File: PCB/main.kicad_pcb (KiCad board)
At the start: 2 copper layers, 76.5 x 37.5 mm, 16 parts, among them J1 USB_C_Receptacle, J2 RJ45, J3 USB_C_Receptacle, J4 USB_C_Receptacle, M1 Fan_PC_Chassis, M2 Fan_PC_Chassis, M3 Fan_PC_Chassis, M4 Fan_PC_Chassis, SW1 SW_DPDT_x2, U2 LAN9512i

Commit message: fixing PCB
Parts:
- added R6: R, Resistor_SMD:R_0815_2038Metric, F.Cu at (177.8, 71.8)
- moved J1 22.7 mm to (148.0, 56.8), turned to 180 degrees
- moved J4 12.4 mm to (136.5, 57.0), turned to 180 degrees
- moved J3 12.3 mm to (125.0, 57.0), turned to 180 degrees
- moved J2 2.76 mm to (167.5, 65.3)
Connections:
- J1 pad A5: unconnected-(J1-CC1-PadA5) -> Net-(J1-CC1)
- J1 pad B5: unconnected-(J1-CC2-PadB5) -> Net-(J1-CC2)
- J1 pad S1: unconnected-(J1-SHIELD-PadS1) -> gnd
- J3 pad S1: unconnected-(J3-SHIELD-PadS1) -> gnd
- J4 pad S1: unconnected-(J4-SHIELD-PadS1) -> gnd
- R7 pad 2: unconnected-(R7-Pad2) -> Net-(J1-CC1)
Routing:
- net gnd: track 101.2 -> 301.4 mm, vias 2 -> 6
- net Net-(J4-CC2): track 128.5 -> 27.5 mm
- net Net-(J1-CC2): track 0.00 -> 86.9 mm
- net VBUSUP: track 94.2 -> 52.0 mm, vias 0 -> 2
- net Net-(J1-CC1): track 0.00 -> 35.0 mm, vias 0 -> 2
- net D-DOWN2: track 64.1 -> 34.6 mm, vias 1 -> 0
- net D+DOWN2: track 75.9 -> 47.0 mm
- net D-DOWN1: track 54.7 -> 31.0 mm, vias 1 -> 0
- net D+UP: track 46.3 -> 33.2 mm, vias 0 -> 1
- net Net-(J3-CC2): track 33.4 -> 24.3 mm
- net D+DOWN1: track 59.9 -> 54.7 mm, vias 1 -> 0
- net Net-(U2B-PRTCTL2): track 99.2 -> 95.1 mm
- net Net-(U2B-TXP): track 45.1 -> 48.2 mm
- net Net-(U2B-RXP): track 38.0 -> 35.7 mm
- net unconnected-(R7-Pad2): track 2.04 -> 0.00 mm
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
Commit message: fixing things
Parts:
- added Y2: KC2520Z, Oscillator:Oscillator_SMD_Kyocera_KC2520Z-4Pin_2.5x2.0mm, F.Cu at (157.0, 87.1)
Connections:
- U2 pad 61: unconnected-(U2A-XI-Pad61) -> Net-(U2A-XI)
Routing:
- net VBUSUP: track 52.0 -> 107.4 mm, vias 2 -> 6
- net Net-(U2A-XI): track 0.00 -> 39.3 mm, vias 0 -> 2
- net gnd: track 301.4 -> 308.6 mm
- net Net-(U2B-USBRBIAS): track 52.5 -> 51.3 mm
- net Net-(U2B-PRTCTL2): track 95.1 -> 95.9 mm

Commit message: fixing lots of things
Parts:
- removed J2: RJ45, Connector_RJ:RJ45_Amphenol_54602-x08_Horizontal
- added C1: 0.1 pF, Capacitor_SMD:C_0201_0603Metric, F.Cu at (138.2, 69.2)
- added C10: 0.1, Capacitor_SMD:C_0201_0603Metric, F.Cu at (138.8, 79.8)
- added C11: 4.7, Capacitor_SMD:C_0201_0603Metric, F.Cu at (153.7, 83.8)
- added C2: 33 pF, Capacitor_SMD:C_0201_0603Metric, F.Cu at (138.0, 70.8)
- added C3: 0.1, Capacitor_SMD:C_0201_0603Metric, F.Cu at (169.2, 81.0)
- added C4: 0.1, Capacitor_SMD:C_0201_0603Metric, F.Cu at (154.8, 77.1)
- added C5: 0.1 uF, Capacitor_SMD:C_0201_0603Metric, F.Cu at (125.7, 62.5)
- added C6: 330, Capacitor_SMD:C_0201_0603Metric, F.Cu at (147.8, 63.8)
- added C8: 1.0, Capacitor_SMD:C_0201_0603Metric, F.Cu at (135.8, 73.8)
- added C9: 0.1, Capacitor_SMD:C_0201_0603Metric, F.Cu at (154.2, 80.8)
- added FB1: FerriteBead, Inductor_SMD:L_Ferrocore_DLG-0302, F.Cu at (158.8, 67.2)
- added J6: RJ45_Amphenol_RJMG1BD3B8K1ANR, Connector_RJ:RJ45_Amphenol_RJMG1BD3B8K1ANR, F.Cu at (176.9, 65.4)
- added R10: 10, Resistor_SMD:R_0201_0603Metric, F.Cu at (168.5, 74.0)
- added R11: 10, Resistor_SMD:R_0201_0603Metric, F.Cu at (165.7, 72.0)
- added R12: 10, Resistor_SMD:R_0201_0603Metric, F.Cu at (153.6, 69.0)
- added R13: 10, Resistor_SMD:R_0201_0603Metric, F.Cu at (176.1, 71.5)
- added R14: 10, Resistor_SMD:R_0201_0603Metric, F.Cu at (169.2, 76.5)
- added R15: 330, Resistor_SMD:R_0201_0603Metric, F.Cu at (125.5, 56.3)
- added R16: 0.1 uF, Resistor_SMD:R_0201_0603Metric, F.Cu at (147.8, 62.8)
- added R17: 39.2 K, Resistor_SMD:R_0201_0603Metric, F.Cu at (146.7, 84.5)
- added R18: 61.9 K, Resistor_SMD:R_0201_0603Metric, F.Cu at (138.5, 83.3)
- added R8: 1.0 M, Resistor_SMD:R_0201_0603Metric, F.Cu at (143.2, 71.5)
- added R9: 12.4k, Resistor_SMD:R_0201_0603Metric, F.Cu at (149.2, 71.2)
- R1, R2, R3, R4: value R -> 5.1k; footprint Resistor_SMD:R_0815_2038Metric -> Resistor_SMD:R_0201_0603Metric
- R5: value R -> 12.0 k; footprint Resistor_SMD:R_0815_2038Metric -> Resistor_SMD:R_0201_0603Metric
- R6, R7: footprint Resistor_SMD:R_0815_2038Metric -> Resistor_SMD:R_0201_0603Metric
- moved SW1 61.4 mm to (112.6, 54.8), turned to -90 degrees
- moved M1 41.1 mm to (110.2, 85.4)
- moved R5 33.3 mm to (141.5, 72.2)
- moved R1 31.7 mm to (143.2, 66.2), turned to 180 degrees
- moved R4 30.3 mm to (145.5, 66.2), turned to 180 degrees
- moved R6 26.3 mm to (153.0, 63.0)
- moved Y2 23.6 mm to (140.8, 70.0), turned to 90 degrees
- moved M2 21.6 mm to (119.2, 77.9)
- moved R7 20.8 mm to (156.8, 62.8), turned to 180 degrees
- moved M3 19.6 mm to (119.2, 85.4)
- moved J3 18.8 mm to (143.8, 56.2)
- moved R2 17.7 mm to (127.5, 64.5)
- moved R3 17.5 mm to (134.2, 64.0), turned to 180 degrees
- moved M4 13.9 mm to (110.2, 77.9)
- moved J1 7.26 mm to (155.2, 56.2)
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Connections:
- net Net-(U2A-VDD33A-Pad10) renamed VDD33A
- J3 pad S1: gnd -> Net-(J3-SHIELD)
- J4 pad S1: gnd -> Net-(J4-SHIELD)
- U2 pad 11: VBUSUP -> Net-(U2B-VBUS_DET)
- U2 pad 34: unconnected-(U2A-TEST2-Pad34) -> gnd
- U2 pad 40: unconnected-(U2A-TEST3-Pad40) -> VBUSUP
- U2 pad 48: unconnected-(U2A-VDD18ETHPLL-Pad48) -> Net-(U2A-VDD18ETHPLL)
- U2 pad 50: unconnected-(U2B-EXRES-Pad50) -> Net-(U2B-EXRES)
- U2 pad 62: unconnected-(U2A-VDD18USBPLL-Pad62) -> Net-(U2A-VDD18USBPLL)
- Y2 pad 1: gnd -> Net-(Y2-GND)
- Y2 pad 2: gnd -> Net-(Y2-GND)
- Y2 pad 4: VBUSUP -> Net-(Y2-VCC)
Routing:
- net VDD33A: track 0.00 -> 156.7 mm, vias 0 -> 3
- net Net-(J1-CC2): track 86.9 -> 13.3 mm, vias 0 -> 2
- net Net-(U2B-PRTCTL2): track 95.9 -> 40.8 mm, vias 0 -> 2
- net VBUSUP: track 107.4 -> 157.4 mm, vias 6 -> 7
- net Net-(U2B-USBRBIAS): track 51.3 -> 1.84 mm, vias 2 -> 0
- net Net-(J4-SHIELD): track 0.00 -> 39.6 mm
- net Net-(U2A-VDD18USBPLL): track 0.00 -> 36.4 mm, vias 0 -> 3
- net Net-(J4-CC1): track 38.8 -> 3.12 mm, vias 2 -> 0
- net Net-(U2A-XI): track 39.3 -> 5.29 mm, vias 2 -> 0
- net Net-(J1-CC1): track 35.0 -> 1.85 mm, vias 2 -> 0
- net Net-(J3-SHIELD): track 0.00 -> 28.2 mm, vias 0 -> 2
- net D-DOWN1: track 31.0 -> 51.1 mm, vias 0 -> 4
- net Net-(J6-RCT): track 0.00 -> 18.8 mm, vias 0 -> 1
- net Net-(C10-Pad2): track 24.4 -> 43.0 mm
- net Net-(U2B-VBUS_DET): track 0.00 -> 17.6 mm, vias 0 -> 2
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
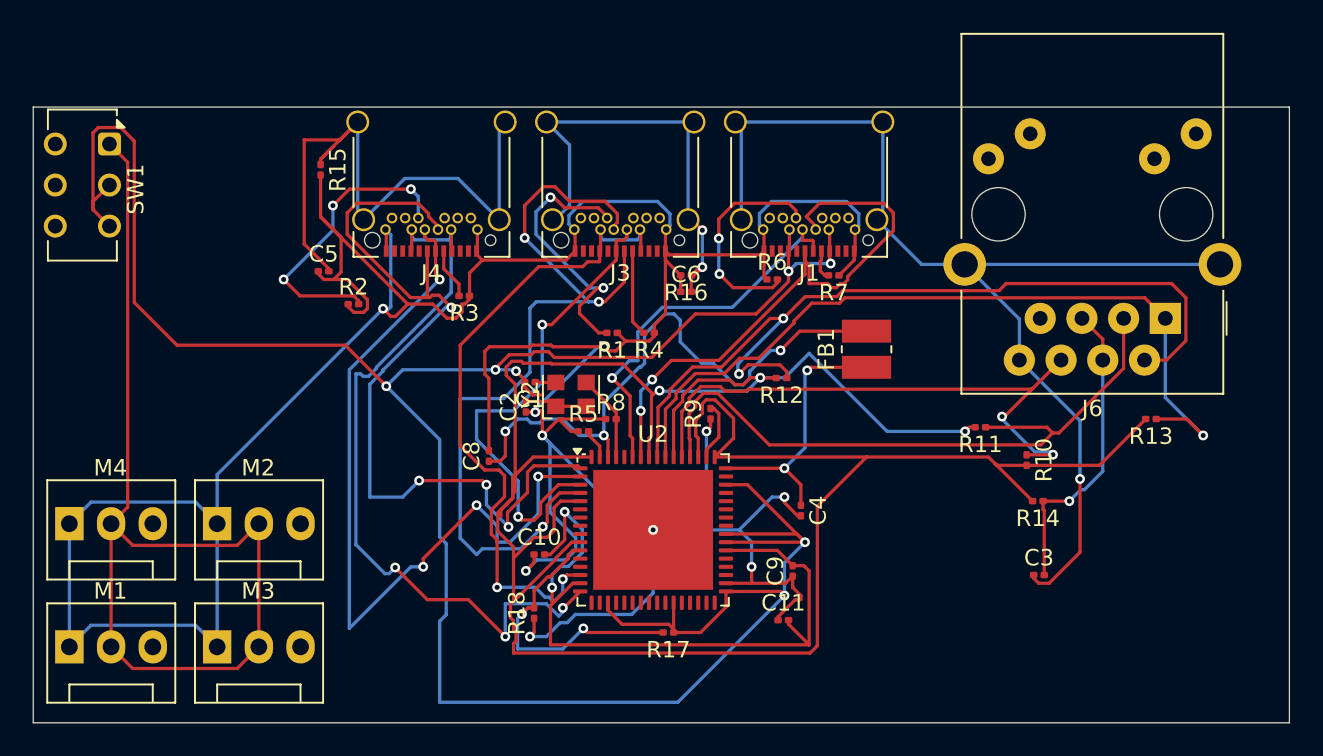
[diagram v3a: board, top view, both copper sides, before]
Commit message: fixing caps
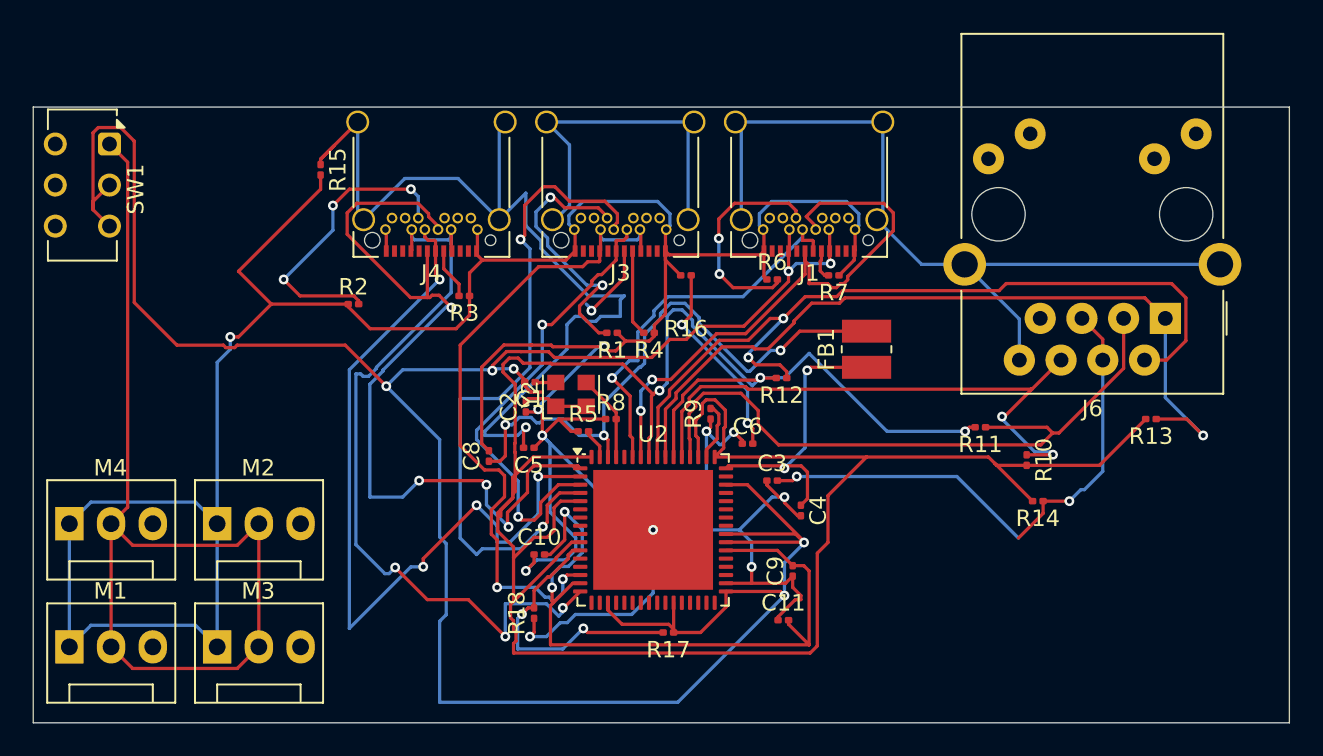
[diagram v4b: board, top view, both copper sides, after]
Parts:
- moved C3 17.2 mm to (153.0, 75.2)
- moved C5 16.5 mm to (138.2, 73.2), turned to 180 degrees
- moved C6 9.98 mm to (151.5, 73.0)
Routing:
- net gnd: track 303.5 -> 280.5 mm
- net Net-(J4-SHIELD): track 39.6 -> 57.4 mm, vias 0 -> 1
- net Net-(J6-RCT): track 18.8 -> 33.4 mm, vias 1 -> 2
- net VDD33A: track 156.7 -> 163.0 mm
- net Net-(J3-SHIELD): track 28.2 -> 34.4 mm
- net D+DOWN2: track 50.8 -> 46.5 mm
- net Net-(J6-TD-): track 52.8 -> 50.9 mm
- net Net-(U2A-VDD18ETHPLL): track 16.5 -> 17.7 mm
- net D-DOWN2: track 29.4 -> 28.2 mm

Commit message: fixing things
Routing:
- net Net-(J6-RCT): vias 2 -> 3
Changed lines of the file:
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@@
+		(net 18)
+	)
+	(via
+		(at 168 78.75)
+		(size 0.6)
+		(drill 0.3)
+		(layers "F.Cu" "B.Cu")
 		(net 18)
 	)

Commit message: fixing things
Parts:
- added C7: 0.1 uF, Capacitor_SMD:C_0201_0603Metric, F.Cu at (151.7, 82.8)
- added R19: 330, Resistor_SMD:R_0201_0603Metric, F.Cu at (151.7, 84.5)
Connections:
- J1 pad S1: gnd -> Net-(J1-SHIELD)
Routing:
- net Net-(J1-SHIELD): track 0.00 -> 99.5 mm, vias 0 -> 1
- net gnd: track 280.5 -> 257.1 mm

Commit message: fixing things
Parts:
- removed J3: USB_C_Receptacle, Connector_USB:USB_C_Receptacle_Amphenol_12401548E4-2A_CircularHoles
- added J2: USB_C_Receptacle, footprintsweeeeee:12401826_AMP, F.Cu at (143.9, 54.1)
- J1, J4: footprint Connector_USB:USB_C_Receptacle_Amphenol_12401548E4-2A_CircularHoles -> footprintsweeeeee:12401826_AMP
- moved J4 2.15 mm to (132.5, 54.1)
- moved J1 2.14 mm to (155.4, 54.1)
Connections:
- C5 pad 2: Net-(J4-SHIELD) -> Net-(C5-Pad2)
- C7 pad 2: Net-(J1-SHIELD) -> Net-(C7-Pad2)
- J1 pad S1: Net-(J1-SHIELD) -> Net-(C7-Pad2)
- J4 pad S1: Net-(J4-SHIELD) -> Net-(C5-Pad2)
- R15 pad 1: Net-(J4-SHIELD) -> Net-(C5-Pad2)
- R19 pad 1: Net-(J1-SHIELD) -> Net-(C7-Pad2)
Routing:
- net Net-(J1-SHIELD): track 99.5 -> 0.00 mm, vias 1 -> 0
- net Net-(C7-Pad2): track 0.00 -> 94.2 mm, vias 0 -> 4
- net Net-(J4-SHIELD): track 57.4 -> 0.00 mm, vias 1 -> 0
- net Net-(C5-Pad2): track 0.00 -> 38.0 mm, vias 0 -> 4
- net VBUSUP: track 157.9 -> 129.3 mm, vias 7 -> 8
- net gnd: track 257.1 -> 282.0 mm
- net D-DOWN1: track 51.1 -> 27.4 mm
- net Net-(U2B-PRTCTL2): track 40.8 -> 61.7 mm
- net D+DOWN1: track 49.1 -> 32.4 mm, vias 4 -> 5
- net D-DOWN2: track 28.2 -> 42.7 mm, vias 2 -> 3
- net Net-(J4-CC2): track 18.2 -> 12.6 mm, vias 3 -> 2
- net Net-(U2A-VDD18USBPLL): track 35.9 -> 41.4 mm
- net Net-(C10-Pad2): track 43.0 -> 37.5 mm
- net D+UP: track 24.1 -> 29.2 mm, vias 1 -> 2
- net VDD33A: track 163.0 -> 159.0 mm
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
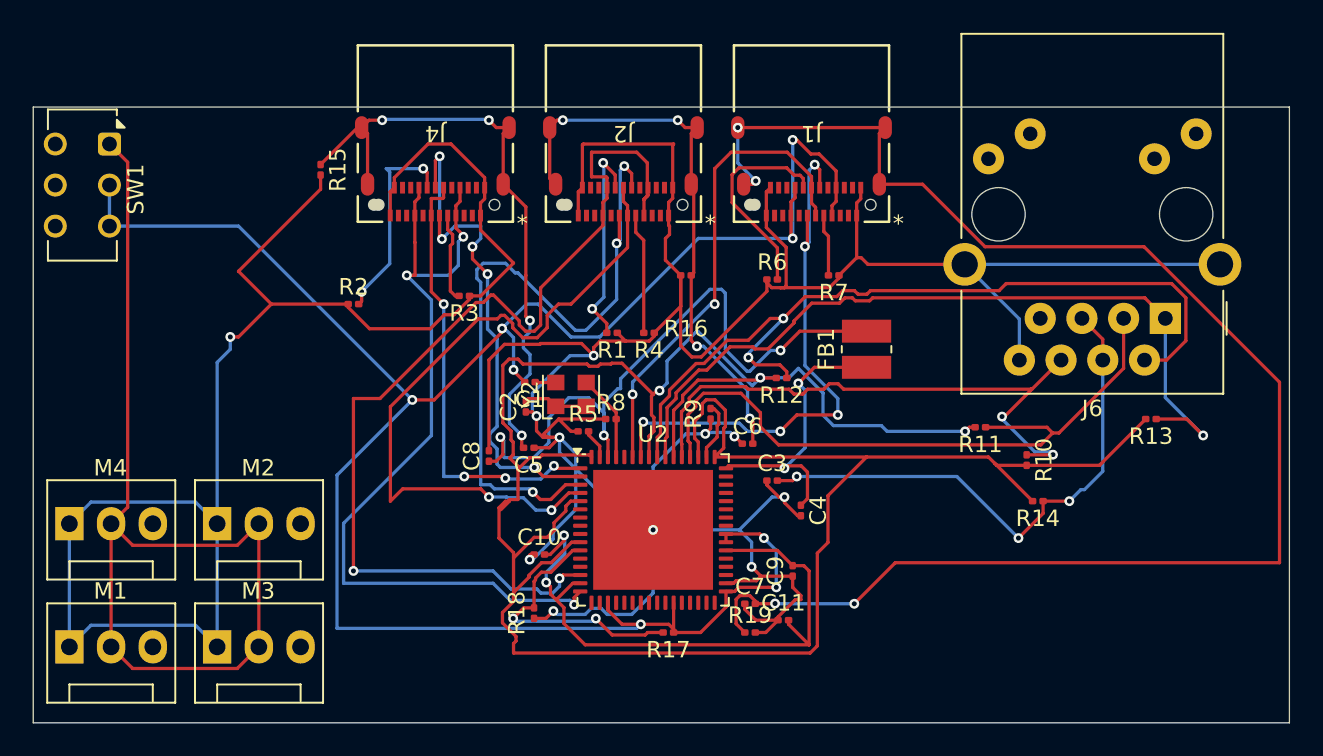
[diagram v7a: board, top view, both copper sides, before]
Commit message: fixing footprints
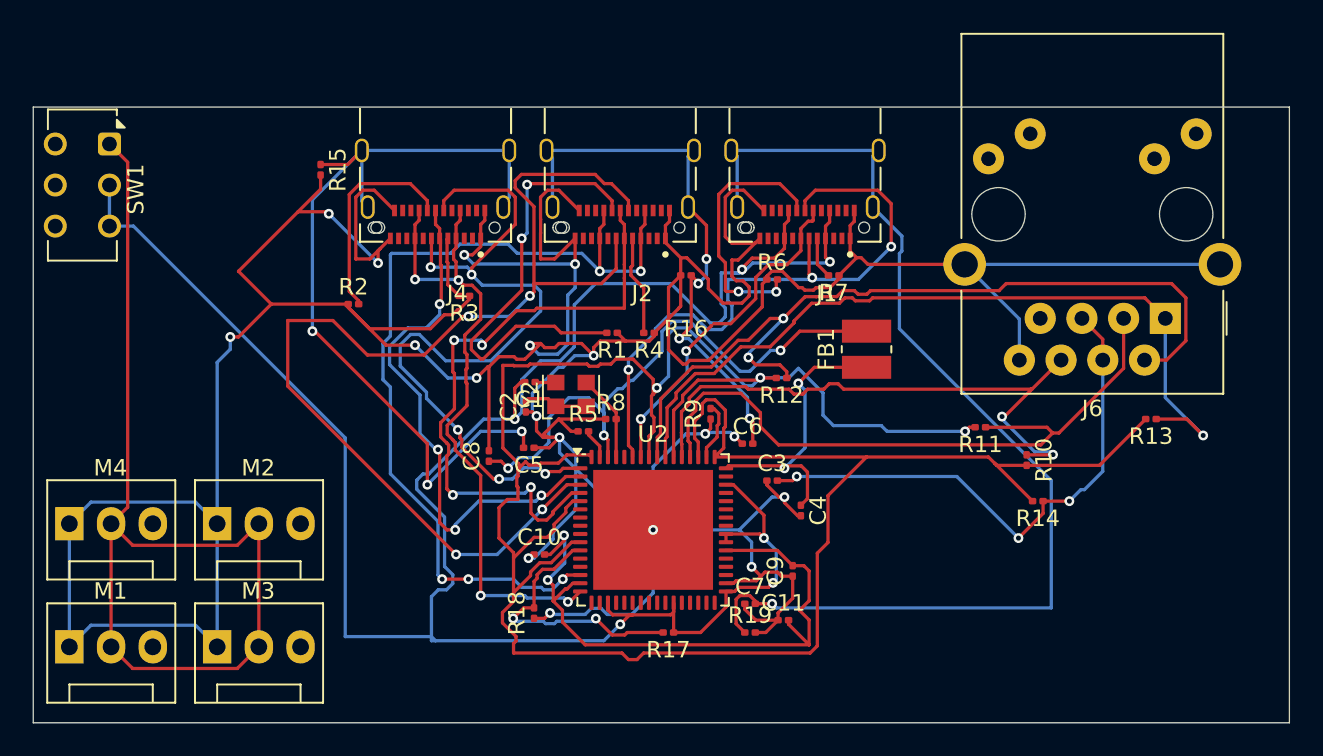
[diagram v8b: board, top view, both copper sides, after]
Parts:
- J1, J2, J4: footprint footprintsweeeeee:12401826_AMP -> footprintsweeeeee:AMPHENOL_12401826E412A
- moved J1 2.17 mm to (155.0, 56.2)
- moved J2 2.14 mm to (143.8, 56.2)
- moved J4 2.14 mm to (132.5, 56.2)
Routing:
- net gnd: track 282.0 -> 317.9 mm, vias 11 -> 18
- net Net-(C7-Pad2): track 94.2 -> 67.2 mm, vias 4 -> 1
- net D-DOWN2: track 42.7 -> 68.1 mm, vias 3 -> 4
- net D-DOWN1: track 27.4 -> 48.7 mm, vias 4 -> 5
- net Net-(J2-CC2): track 12.8 -> 27.2 mm
- net D-UP: track 34.5 -> 20.7 mm, vias 5 -> 2
- net Net-(C5-Pad2): track 38.0 -> 51.8 mm, vias 4 -> 3
- net Net-(U2B-PRTCTL3): track 51.6 -> 39.9 mm, vias 3 -> 4
- net D+UP: track 29.2 -> 39.2 mm, vias 2 -> 3
- net VBUSUP: track 129.3 -> 139.2 mm, vias 8 -> 6
- net Net-(U2B-PRTCTL2): track 61.7 -> 54.3 mm, vias 2 -> 5
- net Net-(U2A-VDD18USBPLL): track 41.4 -> 36.1 mm
- net D+DOWN2: track 42.5 -> 38.3 mm, vias 2 -> 4
- net Net-(J1-CC2): track 12.9 -> 16.0 mm, vias 0 -> 2
- net Net-(J4-CC1): track 5.43 -> 3.82 mm
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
